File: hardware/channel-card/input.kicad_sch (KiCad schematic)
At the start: 57 parts, among them J1 INPUT MODULE, SW1 LOW-CUT (latching), U1 AD8273, U2 NE5532, U3 NE5532, U4 DG413DY

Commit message: Channel card: pot MPNs on the symbols, R184 12k for the RESONANCE pot rating (decision 129)
- Alpha MPNs on RV1 (TRIM), RV181 (CUTOFF), RV301/RV302 (AUX); the Thonk
  -0057 variant suffix is left open
- RV183 reference netlist now SX-POT-012 (Tayda RD901F-40-15K-C10K),
  matching the drawing
- Decision 129: Alpha's RD901F spec rates non-B tapers at 0.02 W; RV183
  carried about 21 mW, R184 10k -> 12k gives about 17 mW (max Q current
  about 254 uA, provisional with R120/R170)
- RD901F spec facts in parts.csv; master STATUS notes RV402 RELEASE at
  about 20.2 mW for its own session

Netlists match, ERC 0/0.

Co-Authored-By: Claude Opus 5.5 <noreply@anthropic.com>
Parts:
- RV1: MPN (none) -> RD902F-40-15K-A100K-0057

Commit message: Channel card: cost levers (decisions 139-143)
- U303 DG412 -> DG413, SC send on the NC section (139)
- All values E24 with JLCPCB fee-free parts; E24 pairs for V/oct
  and fader law, meter ladder re-fitted (140)
- Filter temperature compensation to the backlog (141)
- MUTE/DUCK switched by the buttons' spare pole, U206 DG413 removed;
  100k hold resistors, no dependence on contact sequence (142)
- TL072 difference receiver with 10k 0.1 % instead of the AD8273 (143)
- Trimmers from Mouser, CUTOFF pot from Tayda A-4730
- Breadboard tests 11 (X5R coupling caps) and 12 (fixed V/oct)
- costs.py estimate, 4 channels: EUR 1,035 -> 946

Co-Authored-By: Claude Opus 5.5 <noreply@anthropic.com>
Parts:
- removed U1: AD8273, Package_SO:SOIC-14_3.9x8.7mm_P1.27mm, symbol syntsamix:AD8273
- added R19, R20, R21, R22, R23, R24, R25, R26: 10k, Resistor_SMD:R_0805_2012Metric, symbol Device:R
- added U1: TL072, Package_SO:SOIC-8_3.9x4.9mm_P1.27mm, symbol Amplifier_Operational:TL072
- R1, R2, R3, R4: value 100 -> 10k; MPN (none) -> RT0805BRD0710KL; Manufacturer (none) -> YAGEO; Note (none) -> 0.1 %: receiver resistor match sets the CMRR (decision 143); ProjectPN SX-R-001 -> SX-R-107; Supplier (none) -> LCSC; SupplierPN (none) -> C110775
- R10, R9: value 1k87 -> 1k8; ProjectPN SX-R-079 -> SX-R-101
- R5, R6: value 4k02 -> 3k9; ProjectPN SX-R-038 -> SX-R-099
- R7, R8: value 806 -> 820; ProjectPN SX-R-088 -> SX-R-100
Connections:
- net +15V: now also U1.8 (V+)
- net -15V: now also U1.4 (V-)
- net AGND: now also R22.1, R26.1
- net at C5.1, TP1.1: now also R20.2, U1.1
- net at C2.1, R2.2: now also R21.1
- net at C4.1, R4.2: now also R25.1
- net at C1.1, R1.2: now also R19.1
- net at C6.1, TP4.1: now also R24.2, U1.7
- net at C3.1, R3.2: now also R23.1
- new net: R19.2, R20.1, U1.2 (-)
- new net: R23.2, R24.1, U1.6 (-)
- new net: R25.2, R26.2, U1.5 (+)
- new net: R21.2, R22.2, U1.3 (+)
- no-connect marks 6 -> 4

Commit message: Buttons: SX-SW-001 is the latching GPBS850L, not the momentary GPBS850N
Electrokit 41012905 (on-on, latching) links the GPBS850N datasheet, which
is the momentary twin (Electrokit 41015527, Mouser "Non-Latching ON-(ON)");
the MPN was copied from that file. The latching part is CW GPBS850L
(datasheet Rev 2, 2014: same body, pin grid and pressed = 2-3, 5-6 contacts;
plunger 4.0 mm instead of 3.8).

MPN and footprint name corrected on all 17 button symbols, the generator
scripts and the input reference; parts.csv gets the GPBS850L datasheet and
RoHS source (Mouser 629-GPBS-850L, DigiKey CW179-ND); prices.csv gets the
Electrokit price (6.48 SEK ex VAT at 25+). Erratum on decision 75, checklist
item for the delivered switches and cap sizing, correction notes in the
RoHS audit and the cost review. No wiring change; ERC 0/0 on both cards.
Estimate €769 / €1,037 / €1,609 for 4 / 8 / 16 channels.

Co-Authored-By: Claude Opus 5.5 <noreply@anthropic.com>
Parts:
- SW1: footprint syntsamix:SW_Latching_8.5x8.5mm_CW_GPBS850N -> syntsamix:SW_Latching_8.5x8.5mm_CW_GPBS850L; MPN GPBS850N -> GPBS850L
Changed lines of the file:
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@@
 		(comment 1 "TL072 difference receiver G=1/2, 10k 0.1 % (decision 143), wired inverting; trim stage inverts back (net non-inverting)")
 		(comment 2 "Trim -20..+20 dB overall, 6V2 zener soft clip; 100 Hz 12 dB/oct low-cut via DG413")
-		(comment 3 "Buttons CW GPBS850N: pressed = pins 2-3 and 5-6 closed (datasheet Rev 1)")
+		(comment 3 "Buttons CW GPBS850L: pressed = pins 2-3 and 5-6 closed (datasheet Rev 2)")
 	)
 	(junction
@@
 			)
 		)
-		(property "Footprint" "syntsamix:SW_Latching_8.5x8.5mm_CW_GPBS850N"
+		(property "Footprint" "syntsamix:SW_Latching_8.5x8.5mm_CW_GPBS850L"
 			(at 127 254 0)
 			(hide yes)
@@
 			)
 		)
-		(property "MPN" "GPBS850N"
+		(property "MPN" "GPBS850L"
 			(at 127 254 0)
 			(hide yes)

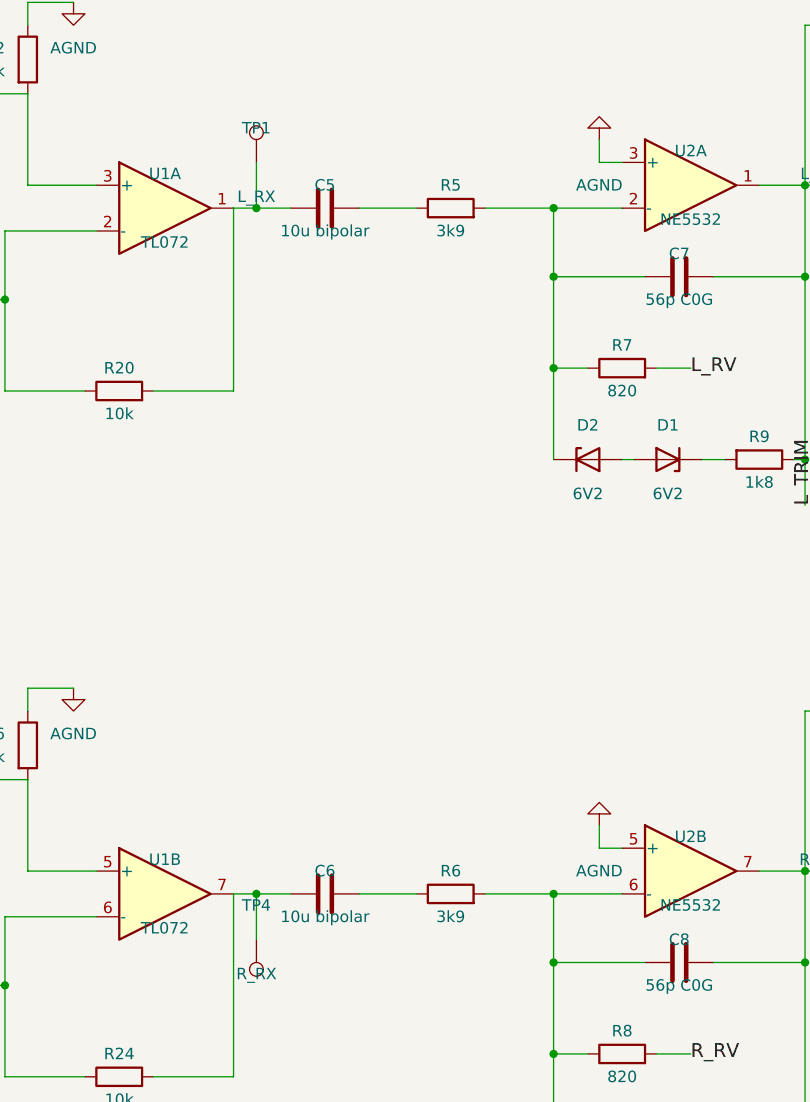
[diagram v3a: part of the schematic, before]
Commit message: Channel card: coupling capacitors as back-to-back ROQANG pairs (decision 161)
Each 10 uF bipolar coupling capacitor (Panasonic EEE-1VA100NP, out of stock
at LCSC and consigned) becomes two ROQANG RVT1V100M0505 10 uF 35 V (SX-C-024,
already on the card) in series, negative to negative: C5+C21, C6+C22,
C101+C108, C151+C158, C107+C109, C157+C159, C221+C235, C271+C285. No new fee
type, nothing on the channel card consigned. Netlists match (input 48,
filter 85, level 43 nets), ERC 0/0. Breadboard test 11 now checks the pair;
the X5R option is dropped. Estimate EUR 778 -> 768 for 4 channels; the
master follows in its own session.

Co-Authored-By: Claude Opus 5.5 <noreply@anthropic.com>
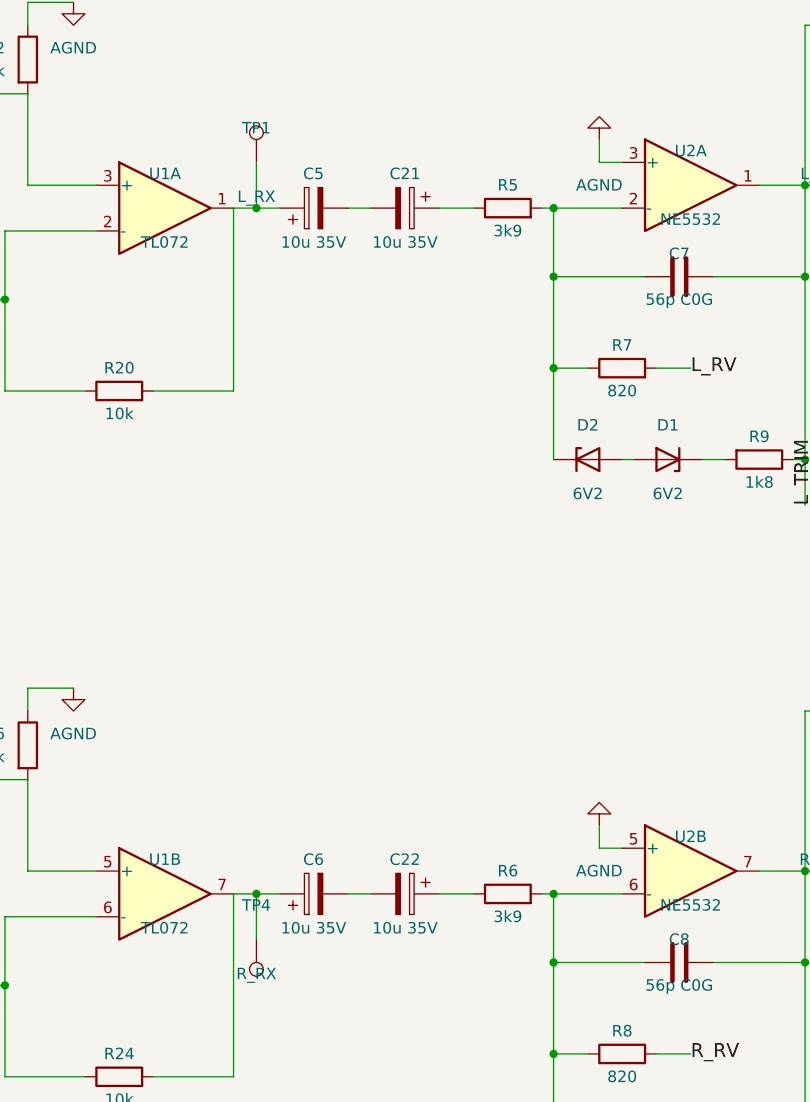
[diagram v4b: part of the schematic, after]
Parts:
- removed C5, C6: 10u bipolar, Capacitor_SMD:C_Elec_6.3x5.4, symbol Device:C
- added C21, C22, C5, C6: 10u 35V, Capacitor_SMD:CP_Elec_5x5.4, symbol Device:C_Polarized
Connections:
- net at R20.2, TP1.1, U1.1: now also C5.1
- net at R24.2, TP4.1, U1.7: now also C6.1
- net at R6.1: now also C22.1
- net at R5.1: now also C21.1
- new net: C22.2, C6.2
- new net: C21.2, C5.2

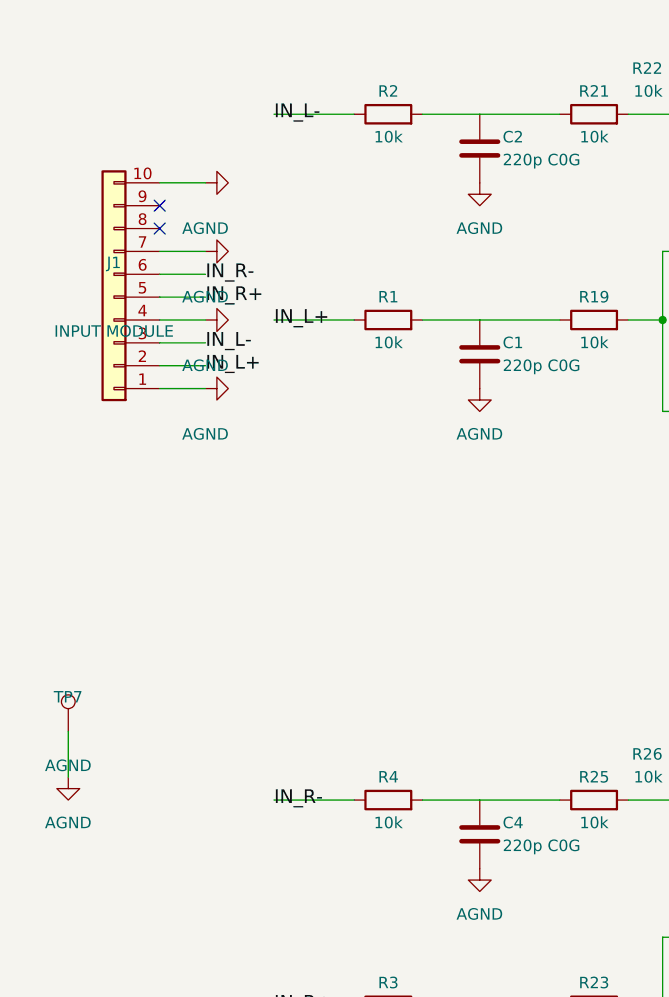
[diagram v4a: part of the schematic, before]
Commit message: Channel card: input header J1 redrawn as the Adam Tech 2x6 box header, pinout of decision 181
Stock KiCad Conn_02x06_Odd_Even and IDC-Header_2x06_P2.54mm_Vertical; DO_L/DO_R open;
opt-in field_at in post_wired.py; netlists match, ERC 0/0.

Co-Authored-By: Claude Opus 5.5 <noreply@anthropic.com>
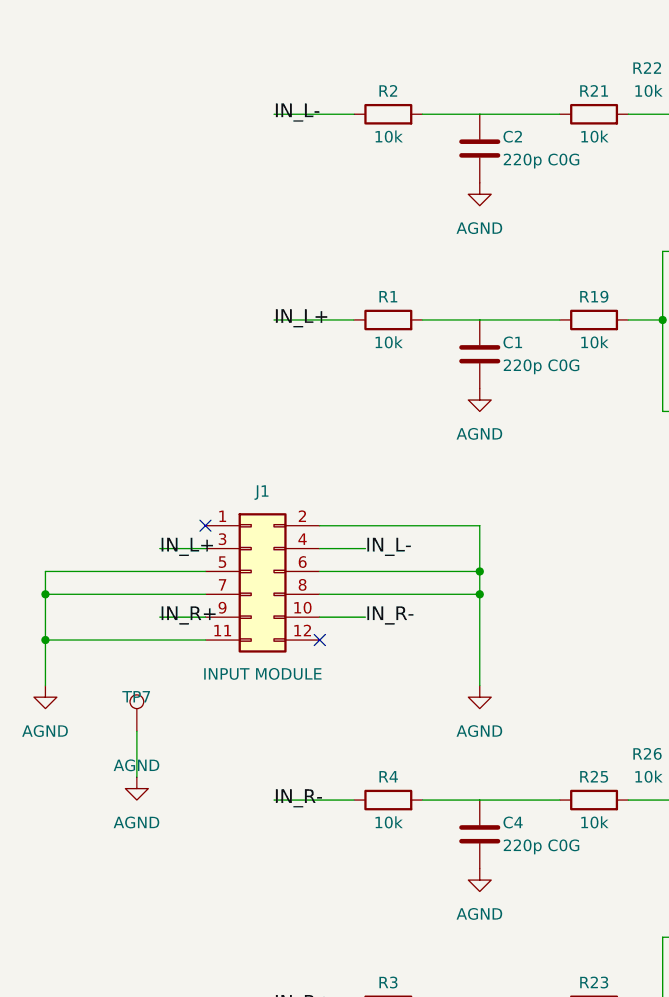
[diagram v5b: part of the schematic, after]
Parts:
- removed J1: INPUT MODULE, Connector_Molex:Molex_KK-254_AE-6410-10A_1x10_P2.54mm_Vertical, symbol Connector_Generic:Conn_01x10
- added J1: INPUT MODULE, Connector_IDC:IDC-Header_2x06_P2.54mm_Vertical, symbol Connector_Generic:Conn_02x06_Odd_Even
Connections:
- net AGND: now also J1.11 (Pin_11), J1.2 (Pin_2), J1.5 (Pin_5), J1.6 (Pin_6), J1.7 (Pin_7), J1.8 (Pin_8)
- net IN_L+: now also J1.3 (Pin_3)
- net IN_L-: now also J1.4 (Pin_4)
- net IN_R+: now also J1.9 (Pin_9)
- net IN_R-: now also J1.10 (Pin_10)
